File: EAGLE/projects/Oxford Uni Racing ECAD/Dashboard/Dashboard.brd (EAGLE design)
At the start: 165.1 x 153.3 mm, 3 parts, among them J1 T821108A1S100CEU, K1 EC2-12NU, K2 EC2-12NU

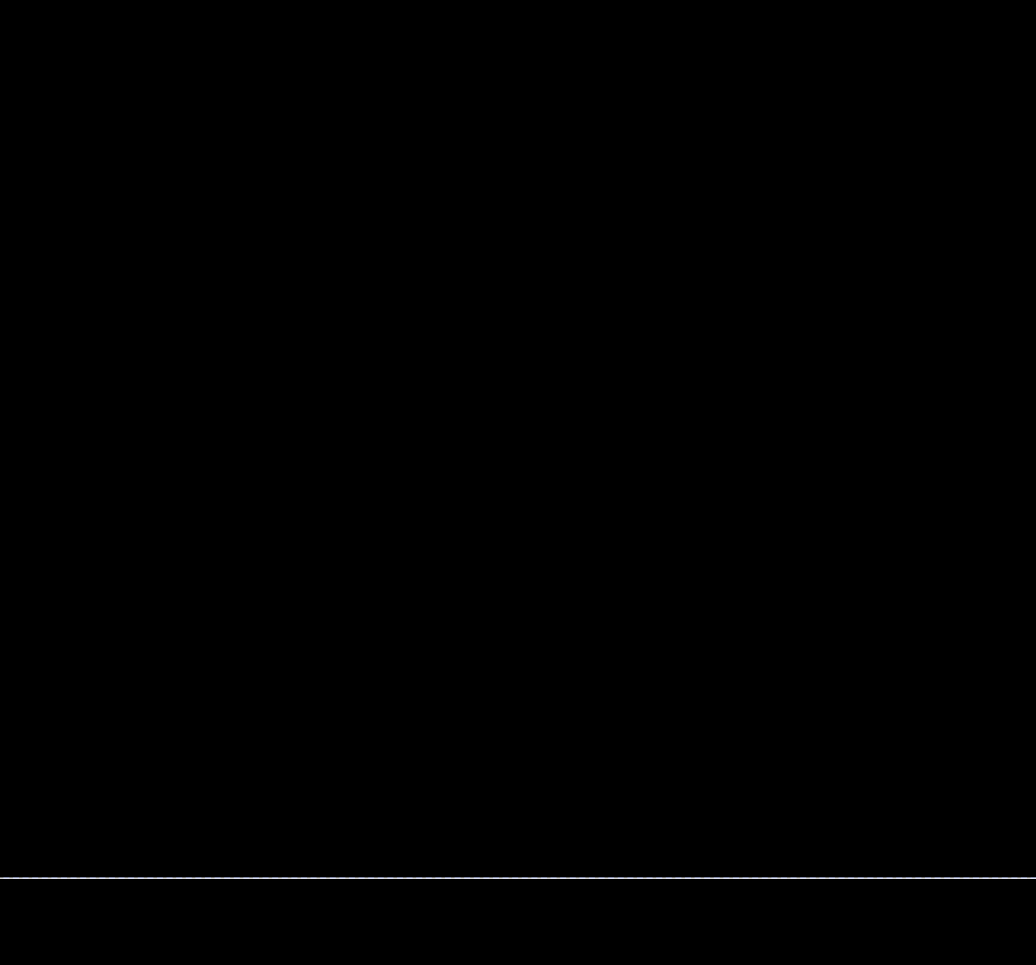
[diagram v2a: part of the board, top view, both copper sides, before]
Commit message: added CAN connector to dashboard
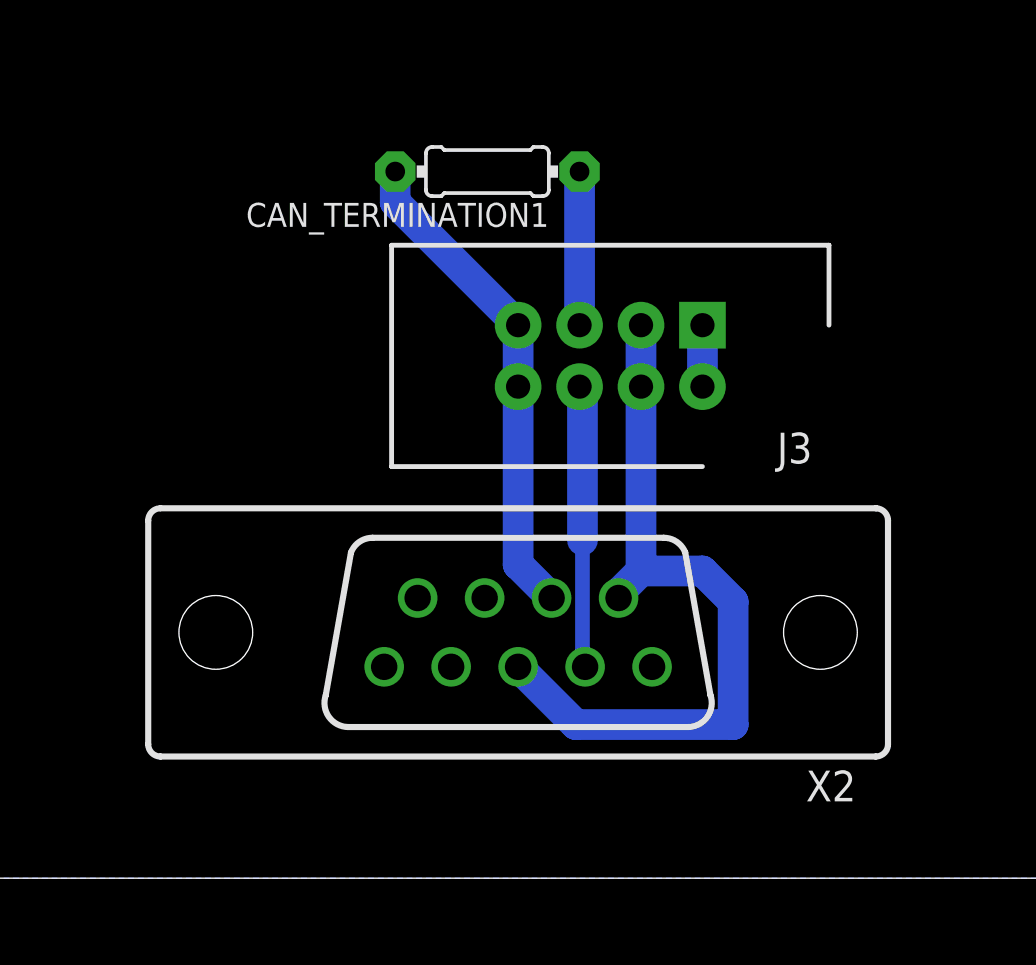
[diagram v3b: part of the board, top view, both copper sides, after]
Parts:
- added CAN_TERMINATION1: 120, adafruit:0204/7
- added J3: T821108A1S100CEU, T821108A1S100CEU:HDRV8W64P254_2X4_1778X895X915P
- added X2: D-SUB9-H2M09ST, con-thomas-betts:H2M09ST
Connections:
- new net 5V: X2.9
- new net CANH: CAN_TERMINATION1.2, J3.7, J3.8, X2.7
- new net CANL: CAN_TERMINATION1.1, J3.5, J3.6, X2.2
- net 12V: now also J3.1, J3.2
- net GND: now also J3.3, J3.4, X2.3, X2.6
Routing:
- net GND: track 45.8 -> 76.8 mm
- net CANH: track 0.00 -> 20.3 mm
- net CANL: track 0.00 -> 18.9 mm
- net 12V: track 22.7 -> 25.2 mm
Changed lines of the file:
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@@
 <layer number="230" name="230bmp" color="7" fill="1" visible="yes" active="yes"/>
 <layer number="231" name="231bmp" color="7" fill="1" visible="yes" active="yes"/>
+<layer number="232" name="Eagle3D_PG2" color="7" fill="1" visible="yes" active="yes"/>
+<layer number="233" name="Eagle3D_PG3" color="7" fill="1" visible="yes" active="yes"/>
 <layer number="248" name="Housing" color="7" fill="1" visible="yes" active="yes"/>
 <layer number="249" name="Edge" color="7" fill="1" visible="yes" active="yes"/>
@@
 <attribute name="VALUE" x="17.152" y="-2.418" size="1.27" layer="27" align="center"/>
 </element>
+<element name="X2" library="con-thomas-betts" library_urn="urn:adsk.eagle:library:191" package="H2M09ST" package3d_urn="urn:adsk.eagle:package:10567/1" value="D-SUB9-H2M09ST" x="92.71" y="10.16" smashed="yes" rot="R180">
+<attribute name="MF" value="" x="92.71" y="10.16" size="1.778" layer="27" rot="R180" display="off"/>
+<attribute name="MPN" value="" x="92.71" y="10.16" size="1.778" layer="27" rot="R180" display="off"/>
+<attribute name="NAME" x="106.68" y="4.445" size="1.27" layer="25" rot="R180"/>
+<attribute name="OC_FARNELL" value="unknown" x="92.71" y="10.16" size="1.778" layer="27" rot="R180" display="off"/>
+<attribute name="OC_NEWARK" value="unknown" x="92.71" y="10.16" size="1.778" layer="27" rot="R180" display="off"/>
+<attribute name="VALUE" x="98.425" y="4.445" size="1.27" layer="27" rot="R180"/>
+</element>
+<element name="CAN_TERMINATION1" library="adafruit" library_urn="urn:adsk.eagle:library:420" package="0204/7" package3d_urn="urn:adsk.eagle:package:6240596/1" value="120" x="91.44" y="29.21" smashed="yes" rot="R180">
+<attribute name="NAME" x="93.98" y="27.9146" size="0.9906" layer="25" ratio="12" rot="R180"/>
+<attribute name="VALUE" x="93.0656" y="29.6926" size="0.9906" layer="27" ratio="12" rot="R180"/>
+</element>
+<element name="J3" library="T821108A1S100CEU" package="HDRV8W64P254_2X4_1778X895X915P" value="T821108A1S100CEU" x="100.33" y="22.86" smashed="yes" rot="R180">
+<attribute name="DESCRIPTION" value="HEADER, VERTICAL, 2.54MM, 8WAY Amphenol T821 Series, 2.54mm Pitch 8 Way 2 Row Straight PCB Header, Solder Termination, 3A" x="104.14" y="22.86" size="1.778" layer="27" rot="R180" display="off"/>
+<attribute name="HEIGHT" value="9.15mm" x="104.14" y="22.86" size="1.778" layer="27" rot="R180" display="off"/>
+<attribute name="MANUFACTURER_NAME" value="Amphenol" x="104.14" y="22.86" size="1.778" layer="27" rot="R180" display="off"/>
+<attribute name="MANUFACTURER_PART_NUMBER" value="T821108A1S100CEU" x="104.14" y="22.86" size="1.778" layer="27" rot="R180" display="off"/>
+<attribute name="NAME" x="104.14" y="17.78" size="1.27" layer="25" rot="R180" align="center"/>
+<attribute name="RS_PART_NUMBER" value="1702738" x="104.14" y="22.86" size="1.778" layer="27" rot="R180" display="off"/>
+<attribute name="VALUE" x="100.33" y="25.4" size="1.27" layer="27" rot="R180" align="center"/>
+</element>
 </elements>
 <signals>
@@
 <vertex x="165.1" y="114.3"/>
 </polygon>
+<contactref element="X2" pad="3"/>
+<contactref element="X2" pad="6"/>
+<wire x1="97.79" y1="12.7" x2="96.8629" y2="11.7729" width="1.27" layer="16"/>
+<wire x1="96.8629" y1="11.7729" x2="96.8629" y2="11.5824" width="1.27" layer="16"/>
+<wire x1="97.79" y1="12.7" x2="100.33" y2="12.7" width="1.27" layer="16"/>
+<wire x1="100.33" y1="12.7" x2="101.6" y2="11.43" width="1.27" layer="16"/>
+<wire x1="101.6" y1="11.43" x2="101.6" y2="6.35" width="1.27" layer="16"/>
+<wire x1="101.6" y1="6.35" x2="95.0976" y2="6.35" width="1.27" layer="16"/>
+<wire x1="95.0976" y1="6.35" x2="92.71" y2="8.7376" width="1.27" layer="16"/>
+<contactref element="J3" pad="3"/>
+<contactref element="J3" pad="4"/>
+<wire x1="97.79" y1="12.7" x2="97.79" y2="20.32" width="1.27" layer="16"/>
+<wire x1="97.79" y1="20.32" x2="97.79" y2="22.86" width="1.27" layer="16"/>
+<wire x1="20.32" y1="-4.86" x2="92.71" y2="8.7376" width="0" layer="19" extent="1-1"/>
 </signal>
 <signal name="DRIVERSWITCH-">
@@
 <wire x1="7.62" y1="-30.48" x2="2.5972" y2="-25.4572" width="0.8128" layer="16"/>
 <wire x1="2.5972" y1="-25.4572" x2="2.5972" y2="-24.13" width="0.8128" layer="16"/>
+<contactref element="J3" pad="1"/>
+<contactref element="J3" pad="2"/>
+<wire x1="100.33" y1="20.32" x2="100.33" y2="22.86" width="1.27" layer="16"/>
+<wire x1="3.81" y1="-12.92" x2="100.33" y2="20.32" width="0" layer="19" extent="1-1"/>
+</signal>
+<signal name="CANL">
+<contactref element="X2" pad="2"/>
+<wire x1="95.25" y1="14.7717375" x2="95.37065" y2="14.6510875" width="0.6096" layer="16"/>
+<wire x1="95.37065" y1="14.6510875" x2="95.37065" y2="13.97" width="0.6096" layer="16"/>
+<contactref element="CAN_TERMINATION1" pad="1"/>
+<contactref element="J3" pad="5"/>
+<contactref element="J3" pad="6"/>
+<wire x1="95.25" y1="29.21" x2="95.25" y2="22.86" width="1.27" layer="16"/>
+<wire x1="95.25" y1="20.32" x2="95.37065" y2="20.19935" width="1.27" layer="16"/>
+<wire x1="95.37065" y1="20.19935" x2="95.37065" y2="13.97" width="1.27" layer="16"/>
+<wire x1="95.4786" y1="8.7376" x2="95.37065" y2="8.84555" width="0.6096" layer="16"/>
+<wire x1="95.37065" y1="8.84555" x2="95.37065" y2="13.97" width="0.6096" layer="16"/>
+<wire x1="95.25" y1="20.32" x2="95.25" y2="22.86" width="0" layer="19" extent="1-1"/>
+</signal>
+<signal name="CANH">
+<contactref element="X2" pad="7"/>
+<wire x1="94.0943" y1="11.5824" x2="92.71" y2="12.9667" width="1.27" layer="16"/>
+<contactref element="CAN_TERMINATION1" pad="2"/>
+<contactref element="J3" pad="7"/>
+<contactref element="J3" pad="8"/>
+<wire x1="92.71" y1="12.9667" x2="92.71" y2="20.32" width="1.27" layer="16"/>
+<wire x1="92.71" y1="20.32" x2="92.71" y2="22.86" width="1.27" layer="16"/>
+<wire x1="92.71" y1="22.86" x2="87.63" y2="27.94" width="1.27" layer="16"/>
+<wire x1="87.63" y1="27.94" x2="87.63" y2="29.21" width="1.27" layer="16"/>
+</signal>
+<signal name="5V">
+<contactref element="X2" pad="9"/>
 </signal>
 </signals>
@@
 which will not be processed correctly with this version.
 </note>
+<note version="8.2" severity="warning">
+Since Version 8.2, EAGLE supports online libraries. The ids
+of those online libraries will not be understood (or retained)
+with this version.
+</note>
+<note version="8.3" severity="warning">
+Since Version 8.3, EAGLE supports URNs for individual library
+assets (packages, symbols, and devices). The URNs of those assets
+will not be understood (or retained) with this version.
+</note>
+<note version="8.3" severity="warning">
+Since Version 8.3, EAGLE supports the association of 3D packages
+with devices in libraries, schematics, and board files. Those 3D
+packages will not be understood (or retained) with this version.
+</note>
 <note version="8.5" severity="warning">
